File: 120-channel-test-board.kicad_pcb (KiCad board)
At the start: 2 copper layers, 76 x 50.8 mm, 261 parts, among them P1 CONN_01X01, P10 CONN_01X01, P100 CONN_01X01, P101 CONN_01X01, P102 CONN_01X01, P103 CONN_01X01, P104 CONN_01X01, P105 CONN_01X01, P106 CONN_01X01, P107 CONN_01X01, P108 CONN_01X01, P109 CONN_01X01, P11 CONN_01X01, P110 CONN_01X01, P111 CONN_01X01, P112 CONN_01X01, P113 CONN_01X01, P114 CONN_01X01, P115 CONN_01X01, P116 CONN_01X01, P117 CONN_01X01, P118 CONN_01X01, P119 CONN_01X01, P12 CONN_01X01, P120 CONN_01X01, P121 CONN_01X01, P122 CONN_01X01, P123 CONN_01X01, P124 CONN_01X01, P125 CONN_01X01, P126 CONN_01X01, P127 CONN_01X01, P128 CONN_01X01, P129 CONN_01X01, P13 CONN_01X01, P130 CONN_01X01, P131 CONN_01X01, P132 CONN_01X01, P133 CONN_01X01, P134 CONN_01X01, P135 CONN_01X01, P136 CONN_01X01, P137 CONN_01X01, P138 CONN_01X01, P14 CONN_01X01, P15 CONN_01X01, P16 CONN_01X01, P17 CONN_01X01, P18 CONN_01X01, P19 CONN_01X01, P2 CONN_01X01, P20 CONN_01X01, P21 CONN_01X01, P22 CONN_01X01, P23 CONN_01X01, P24 CONN_01X01, P25 CONN_01X01, P26 CONN_01X01, P27 CONN_01X01, P28 CONN_01X01, P29 CONN_01X01, P3 CONN_01X01, P30 CONN_01X01, P31 CONN_01X01, P32 CONN_01X01, P33 CONN_01X01, P34 CONN_01X01, P35 CONN_01X01, P36 CONN_01X01, P37 CONN_01X01, P38 CONN_01X01, P39 CONN_01X01, P4 CONN_01X01, P40 CONN_01X01, P41 CONN_01X01, P42 CONN_01X01, P43 CONN_01X01, P44 CONN_01X01, P45 CONN_01X01, P46 CONN_01X01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

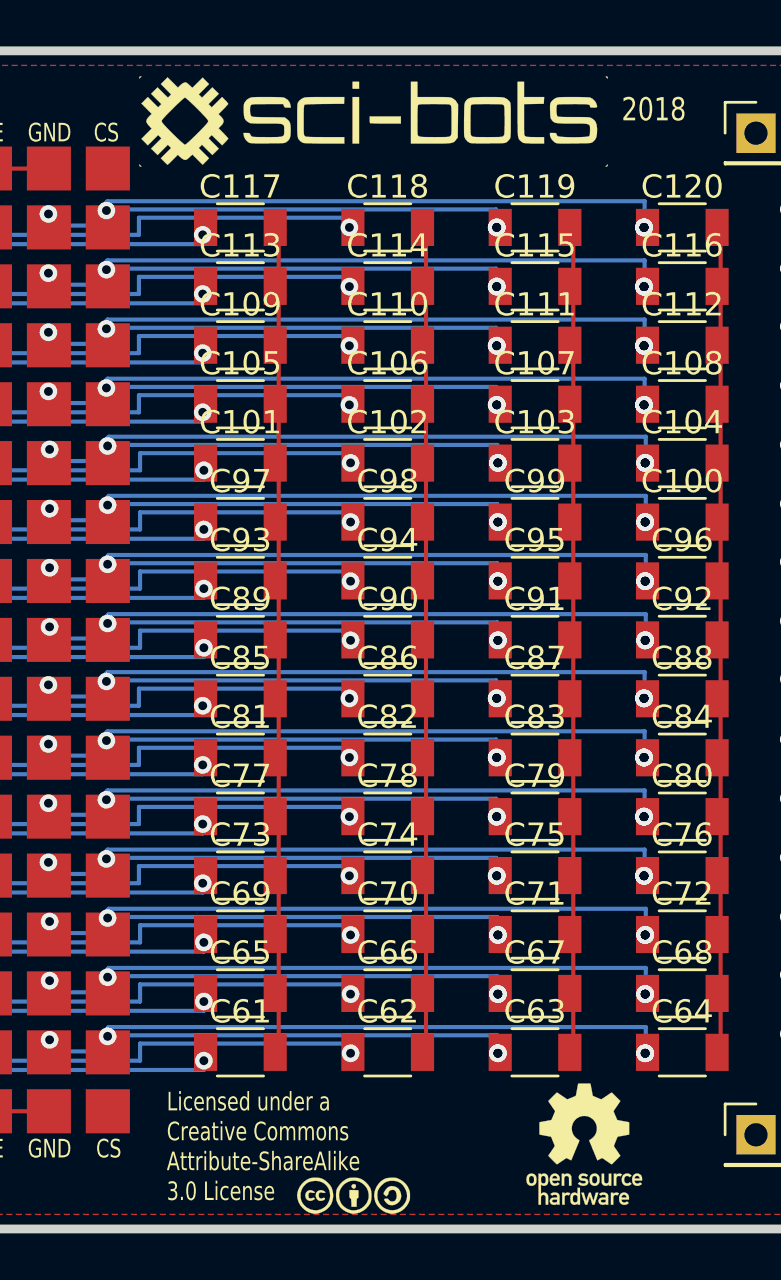
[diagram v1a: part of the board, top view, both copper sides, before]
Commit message: Update pcb from netlist
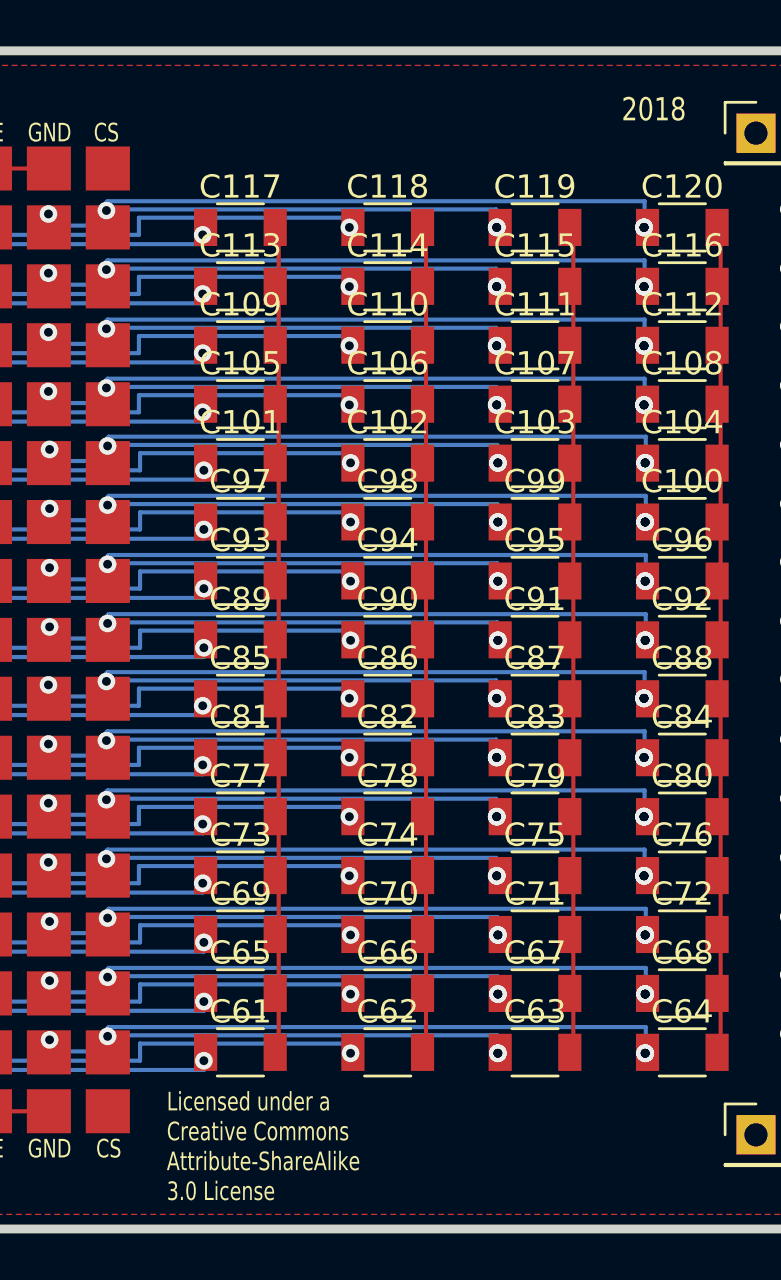
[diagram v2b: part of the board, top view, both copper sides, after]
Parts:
- removed G***: LOGO, Sci-Bots:SCI-BOTS-LOGO
- removed G***: LOGO, Sci-Bots:CC_S_A_logo_5mm
- removed G***: LOGO, Sci-Bots:OSHW_logo_5mm
- P1, P10, P100, P101, P102, P103, P104, P105, P106, P107, P108, P109, P11, P110, P111, P112, P113, P114, P115, P116, P117, P118, P119, P12, P120, P122, P123, P124, P125, P126, P127, P128, P129, P13, P130, P131, P132, P133, P134, P135, P136, P137, P14, P15, P16, P17, P18, P19, P2, P20, P21, P22, P23, P24, P25, P26, P27, P28, P29, P3, P30, P31, P32, P33, P34, P35, P36, P37, P38, P39, P4, P40, P41, P42, P43, P44, P45, P46, P47, P48, P49, P5, P50, P51, P52, P53, P54, P55, P56, P57, P58, P59, P6, P60, P61, P62, P63, P64, P65, P66, P67, P68, P69, P7, P70, P71, P72, P73, P74, P75, P76, P77, P78, P79, P8, P80, P81, P82, P83, P84, P85, P86, P87, P88, P89, P9, P90, P91, P92, P93, P94, P95, P96, P97, P98, P99: footprint wheelerlab:1.9mm_DMF_Electrode -> Sci-Bots:1.9mm_DMF_Electrode
